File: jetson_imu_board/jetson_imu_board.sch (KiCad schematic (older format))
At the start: 12 parts, among them P1 J3A1, P2 J3A2, P3 CONN_01X02, P4 CONN_01X04, P5 CONN_01X06, P6 CONN_01X07, U1 TXB0108

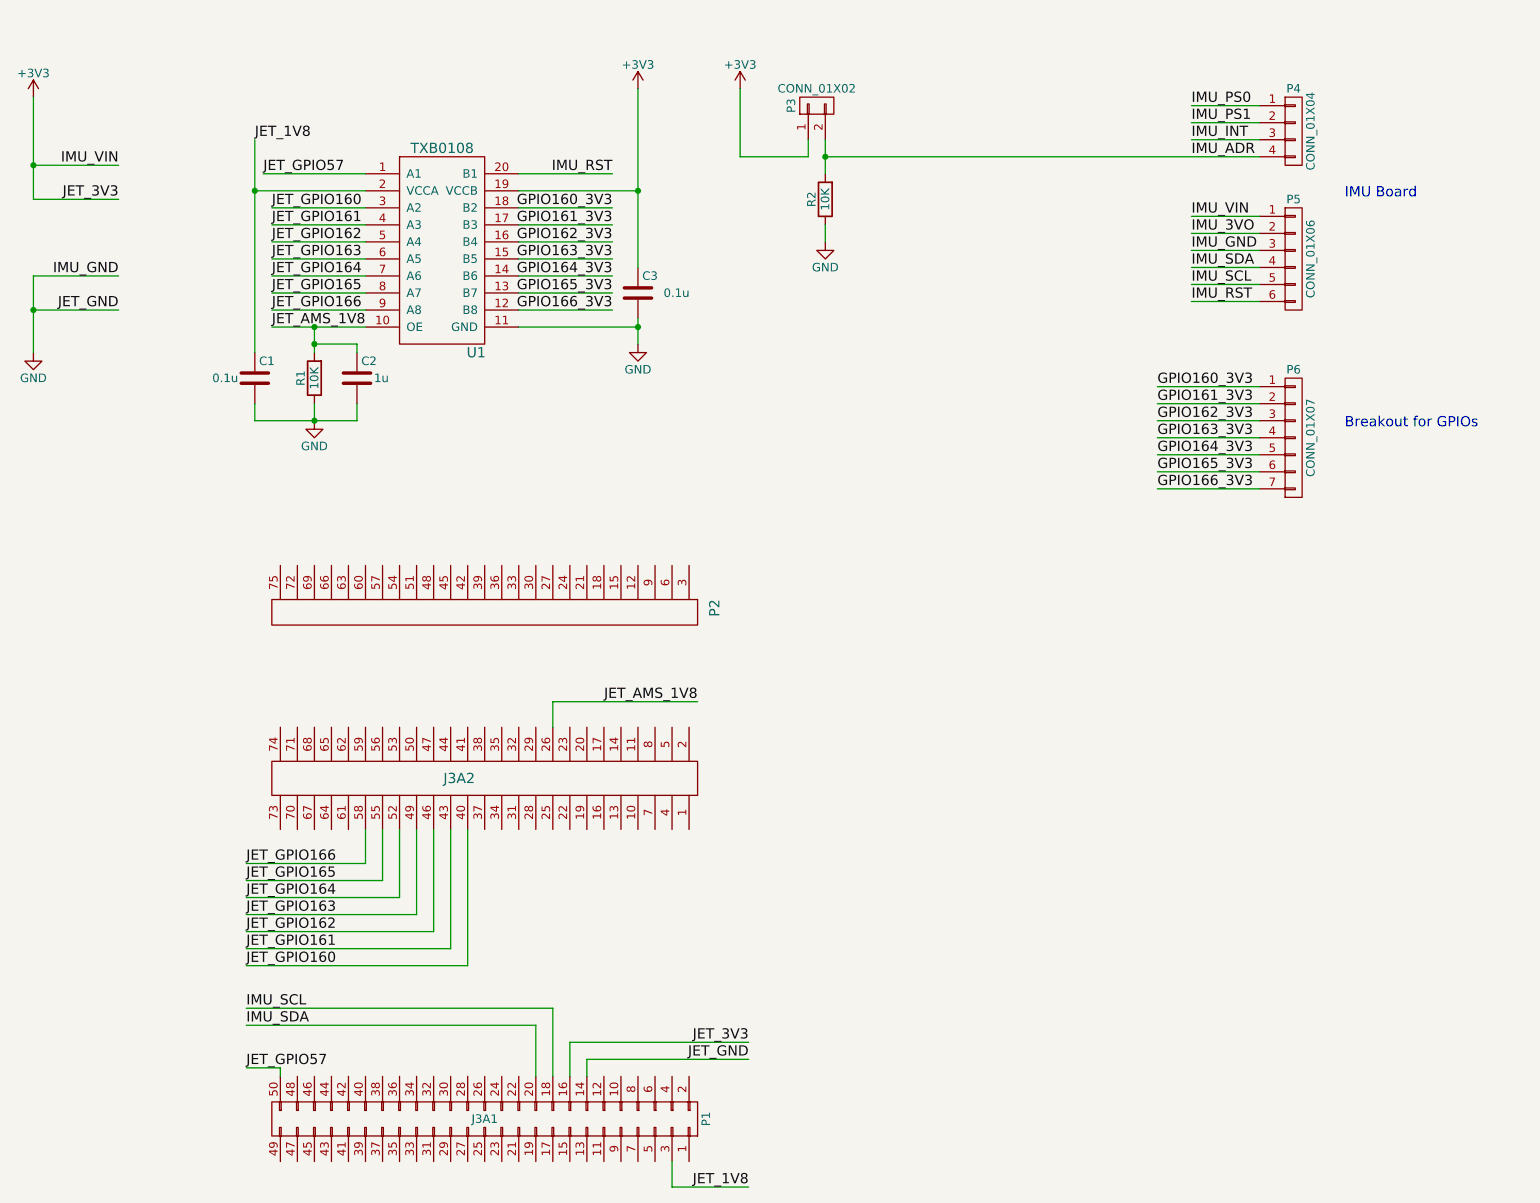
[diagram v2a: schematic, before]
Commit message: Fixed ERC rule violations
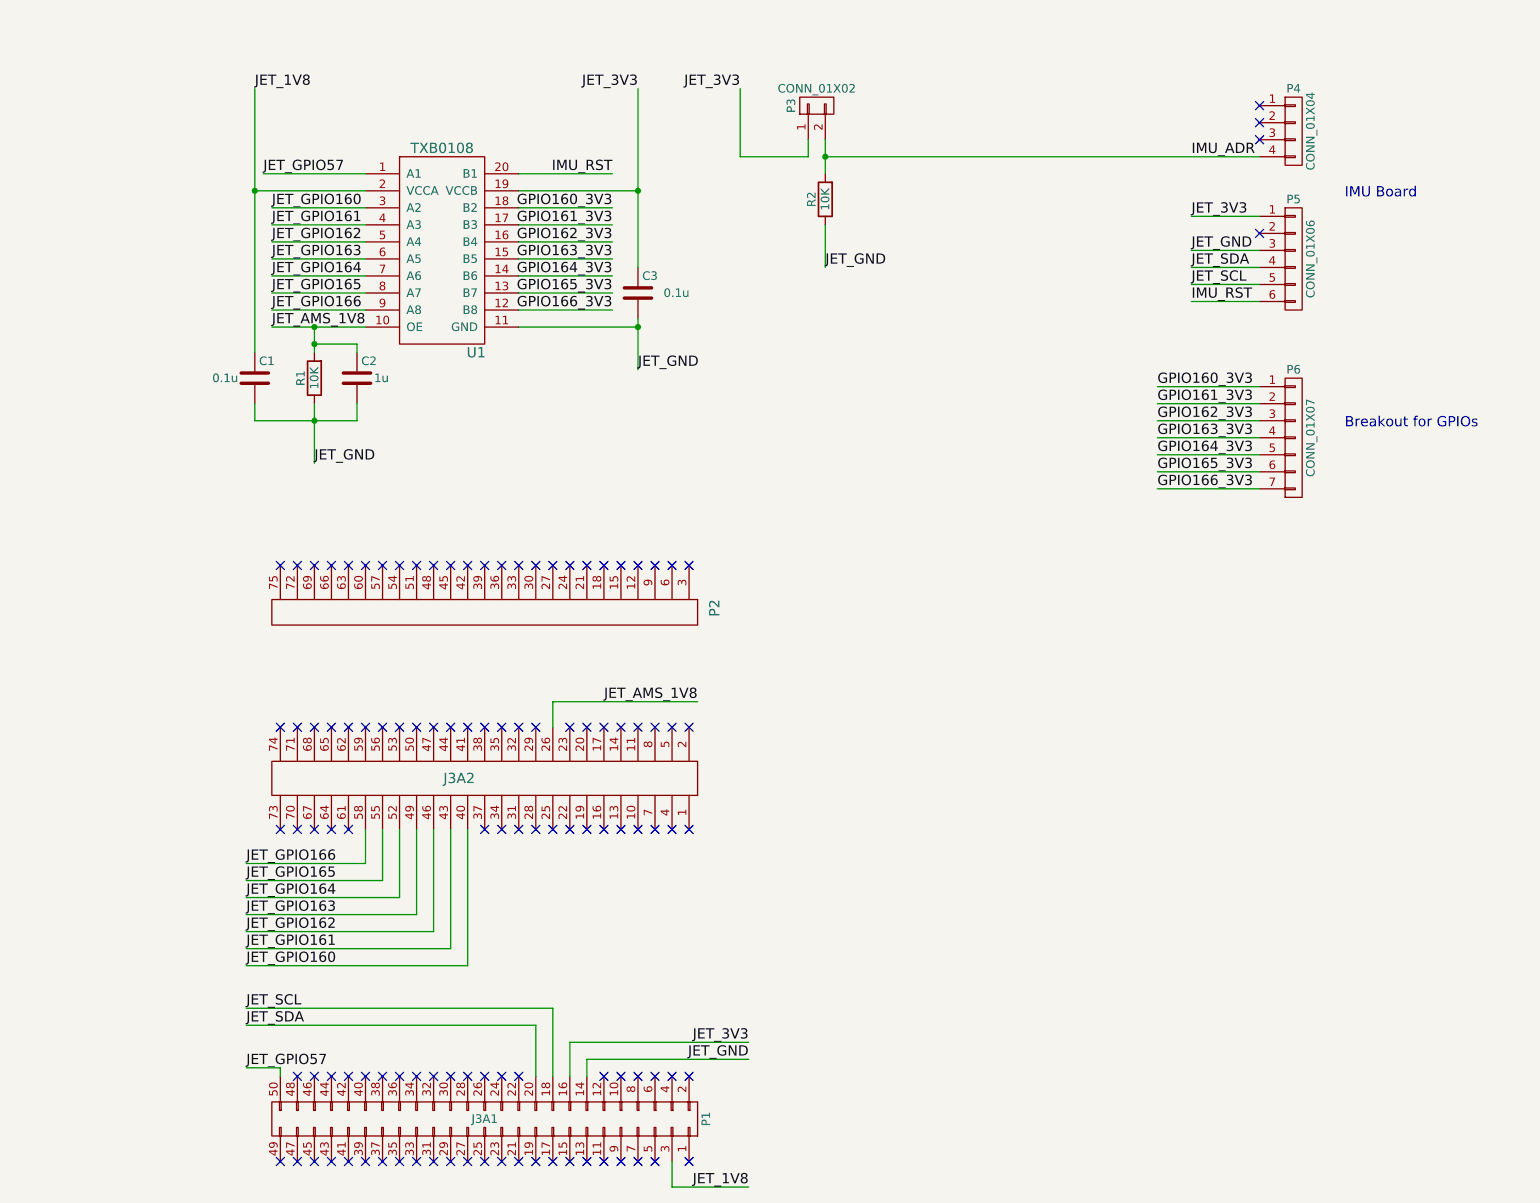
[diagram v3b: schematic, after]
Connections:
- net +3V3 renamed JET_3V3
- net GND renamed JET_GND
- net IMU_3VO: no longer names the net of P5.2 (P2)
- net IMU_INT: no longer names the net of P4.3 (P3)
- net IMU_PS0: no longer names the net of P4.1 (P1)
- net IMU_PS1: no longer names the net of P4.2 (P2)
- net IMU_SCL renamed JET_SCL
- net IMU_SDA renamed JET_SDA
- no-connect marks 0 -> 115

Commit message: Finished routing and layout
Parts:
- P2: footprint Pin_Headers:Pin_Header_Straight_2x25_Pitch2.00mm -> jetson_imu_footprints:Pin_Header_Straight_3x25_Pitch2.00mm
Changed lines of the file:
@@
 F 0 "P2" H 4350 5600 60  0000 C CNN
 F 1 "J3A2" V 3350 4100 60  0000 C CNN
-F 2 "Pin_Headers:Pin_Header_Straight_2x25_Pitch2.00mm" H 4100 1950 60  0001 C CNN
+F 2 "jetson_imu_footprints:Pin_Header_Straight_3x25_Pitch2.00mm" H 4100 1950 60  0001 C CNN
 F 3 "" H 4100 1950 60  0001 C CNN
 	1    3900 4500
